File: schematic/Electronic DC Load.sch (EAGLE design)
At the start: 92 parts, among them J1 POWER_JACKPTH_LOCK, J2 AVR_SPI_PROG_3X22X3_LOCK, Q1 IRFP250NH, Q2 600mA/40V, U1 ATMEGA328P_TQFP, U2 PCF8574_DW_16, U3 REF5050_D_8, U4 INA210AIDCKRG4, U5 MP1584EN, U6 AD8629ARZ, U7 AD7190BRUZ, U8 AD5541ARZ, U9 LM35_LP_3, Y1 16MHz

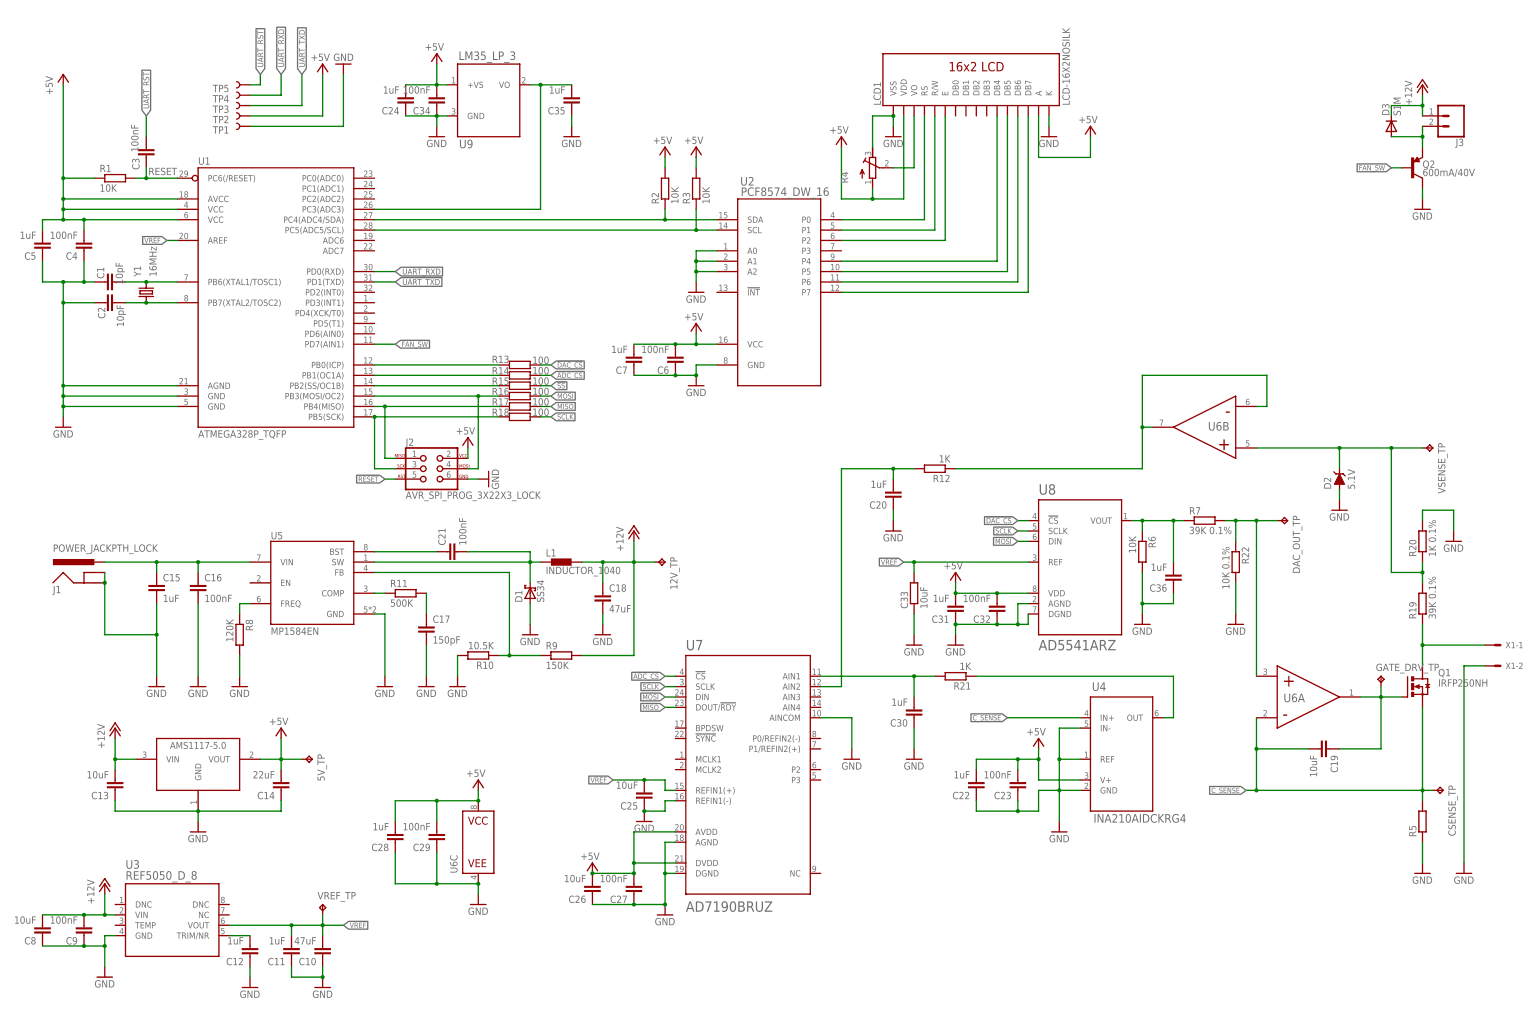
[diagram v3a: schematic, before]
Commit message: Add EC11 Rotary Encoder
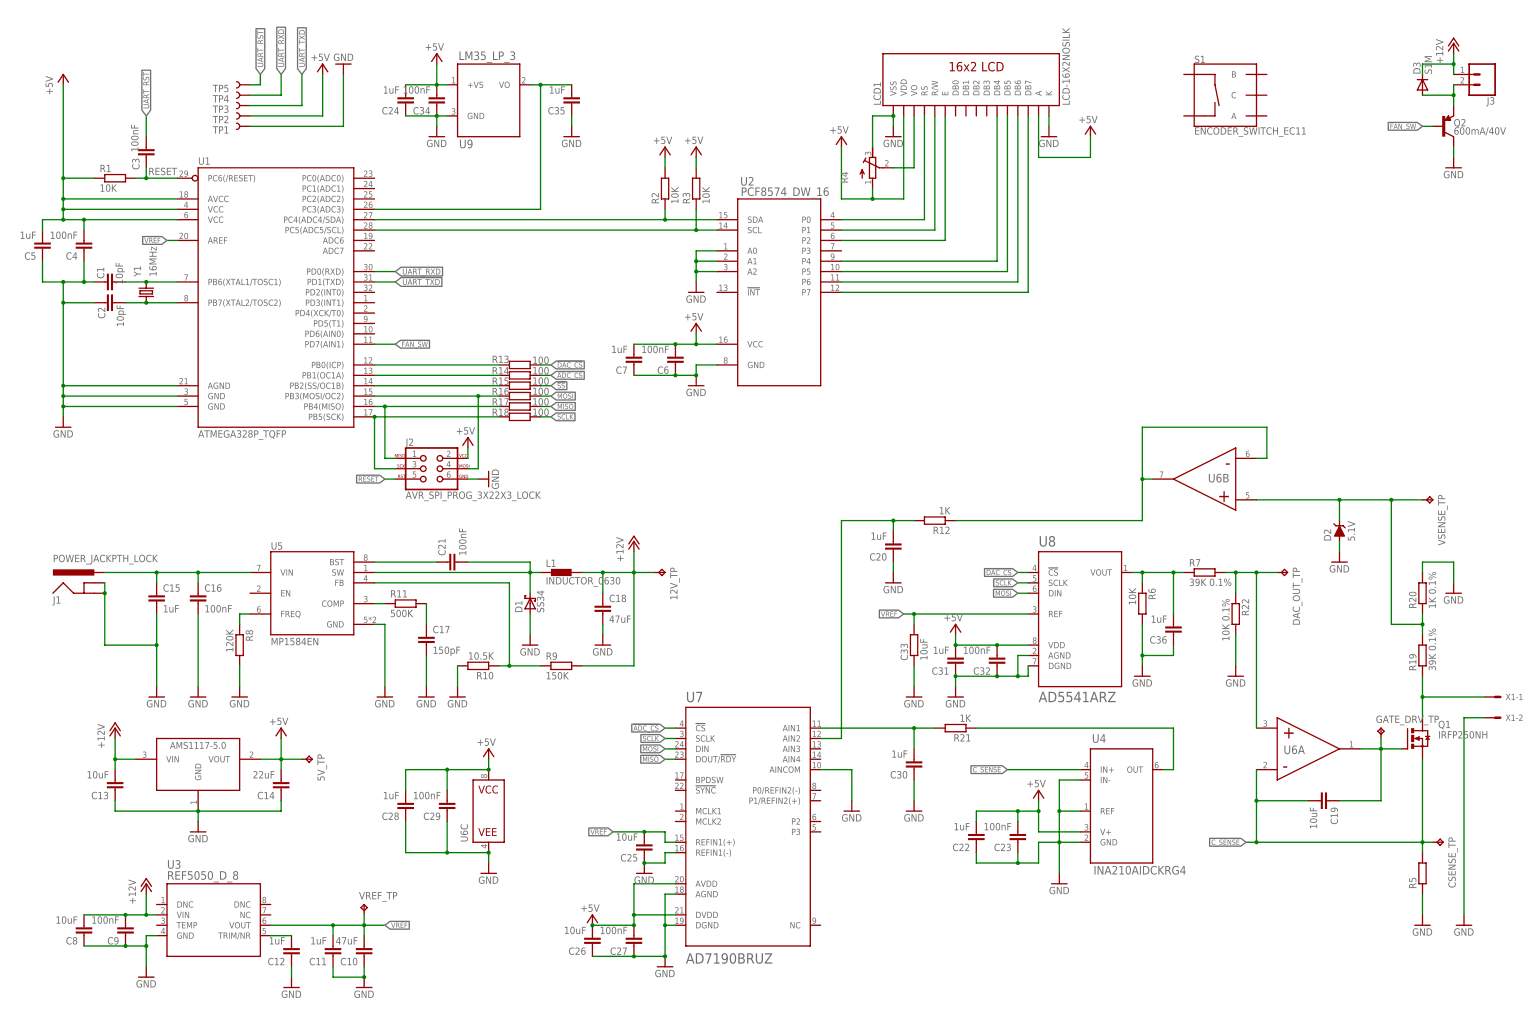
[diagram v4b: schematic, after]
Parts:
- added S1: ENCODER_SWITCH_EC11, 0_discrete:ENCODER_SWITCH_EC11
- L1: value INDUCTOR_1040 -> INDUCTOR_0630; device 0_discrete:INDUCTOR_1040 -> 0_discrete:INDUCTOR_0630
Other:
- moved on the sheet: 12V_TP, C10, C11, C12, C15, C16, C17, C18, C19, C20, C21, C22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

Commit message: First layouts
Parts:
- removed 5V_TP, CSENSE_TP, DAC_OUT_TP, GATE_DRV_TP, VREF_TP, VSENSE_TP: TPB2,54, testpad:TPB2,54
- removed TP1: TEST-POINT2, SparkFun-Connectors:TEST-POINT2
- removed TP2, TP3, TP4, TP5: TEST-POINT3, SparkFun-Connectors:TEST-POINT3
- removed U$1: AMS1117-5.0, AMS1117-5.0:AMS1117-5.0
- removed X1: (no value), con-molex:KK-156-2
- removed Y1: 16MHz, crystal-geyer_V1_0:KX-7
- added J4: KF762-2, 0_discrete:KF762-2
- added Q3: 600mA/40V, SparkFun-DiscreteSemi:TRANS_PNP-MMBT4403
- added R23, R24, R25, R26, R27, R28, R31, R32, R33: 10K, resistor:R-EU_R0603
- added R29, R30: 1K, resistor:R-EU_R0805
- added R34: 1uF, resistor:R-EU_R0805
- added R35: 39K 0.1%, resistor:R-EU_R0805
- added R36: 10K 0.1%, resistor:R-EU_R0805
- added R37: .005, 0_sup:MRE_R005_4W_2728_1%
- added R38: 39K 0.1%, resistor:R-EU_M0805
- added R39: 1K 0.1%, resistor:R-EU_M0805
- added S2, S3, S4, S5: SWITCH_6X6, 0_discrete:SWITCH_6X6
- added U10: AD8629ARZ, 0_analog-devices:AD8629ARZ
- added VR1: 10k, SparkFun-Resistors:TRIMPOT-SMD-3MM-OPEN-1/10W-25%
- C1: value 10pF -> 10uF; device resistor:C-EUC0603 -> resistor:C-EUC1206
- C10: device resistor:C-EUC0603 -> resistor:C-EUC1206
- C11, C34, C4, C5, C6: device resistor:C-EUC0603 -> resistor:C-EUC0805
- C12, C35: value 1uF -> 100nF; device resistor:C-EUC0603 -> resistor:C-EUC0805
- C13, C8: value 10uF -> 1uF; device resistor:C-EUC0603 -> resistor:C-EUC0805
- C14: value 22uF -> 150pF; device resistor:C-EUC0603 -> resistor:C-EUC0402
- C15, C24: value 1uF -> 100nF
- C17: value 150pF -> 1uF; device resistor:C-EUC1206 -> resistor:C-EUC0805
- C18: value 47uF -> 10uF
- C19: value 10uF -> 47uF; device resistor:C-EUC0603 -> resistor:C-EUC1206
- C2: value 10pF -> 100nF
- C20, C28: value 1uF -> 100nF; device resistor:C-EUC0805 -> resistor:C-EUC0603
- C21: device resistor:C-EUC1206 -> resistor:C-EUC0805
- C22: value 1uF -> 10uF; device resistor:C-EUC0805 -> resistor:C-EUC1206
- C23: device resistor:C-EUC0805 -> resistor:C-EUC0603
- C25, C26: value 10uF -> 100nF
- C29: value 100nF -> 1uF
- C3: value 100nF -> 10uF; device resistor:C-EUC0603 -> resistor:C-EUC1206
- C31, C36: value 1uF -> 10uF; device resistor:C-EUC0603 -> resistor:C-EUC1206
- C32, C9: value 100nF -> 1uF; device resistor:C-EUC0603 -> resistor:C-EUC0805
- C33: value 10uF -> 1uF; device resistor:R-EU_M1206 -> resistor:C-EUC0805
- C7: value 1uF -> 22uF; device resistor:C-EUC0603 -> resistor:C-EUC1206
- D1: value SS34 -> DIODE_SCHOTTKEYSS24; device diode:SCHOTTKY-DIODESMC -> 0_discrete:DIODE_SCHOTTKEYSS24
- J2: value AVR_SPI_PROG_3X22X3_LOCK -> AVR_SPI_PROG_3X2PTH; device SparkFun-Connectors:AVR_SPI_PROG_3X22X3_LOCK -> SparkFun-Connectors:AVR_SPI_PROG_3X2PTH
- J3: value (none) -> FAN
- Q1: value IRFP250NH -> 16MHz; device 0_discrete:IRFP250NH -> crystal-geyer_V1_0:KX-7
- Q2: value 600mA/40V -> IRFP250NV; device SparkFun-DiscreteSemi:TRANS_PNP-MMBT4403 -> 0_discrete:IRFP250NV
- R1, R2: value 10K -> 10pF; device resistor:R-EU_R0603 -> resistor:R-EU_R0805
- R10: value 10.5K -> 100; device resistor:R-EU_R0603 -> resistor:R-EU_M0805
- R11: value 500K -> 100; device resistor:R-EU_R0603 -> resistor:R-EU_M0805
- R12, R21: value 1K -> 10K; device resistor:R-EU_R0805 -> resistor:R-EU_R0603
- R13: value 100 -> 150K; device resistor:R-EU_M0805 -> resistor:R-EU_R0603
- R14, R15: value 100 -> 10K
- R16, R17, R18: value 100 -> 10K; device resistor:R-EU_M0805 -> resistor:R-EU_R0603
- R19: value 39K 0.1% -> 10K; device resistor:R-EU_M0805 -> resistor:R-EU_R0603
- R20: value 1K 0.1% -> 10K; device resistor:R-EU_M0805 -> resistor:R-EU_R0603
- R22: value 10K 0.1% -> 10K; device resistor:R-EU_R0805 -> resistor:R-EU_R0603
- R4: value (none) -> 120K; device resistor:R-TRIMM3296P -> resistor:R-EU_R0603
- R5: value (none) -> 500K; device 0_sup:MRE_R005_4W_2728_1% -> resistor:R-EU_R0603
- R6: value 10K -> 10.5K; device resistor:R-EU_R0805 -> resistor:R-EU_R0603
- R7: value 39K 0.1% -> 100; device resistor:R-EU_R0805 -> resistor:R-EU_M0805
- R8: value 120K -> 100; device resistor:R-EU_R0603 -> resistor:R-EU_M0805
- R9: value 150K -> 100; device resistor:R-EU_R0603 -> resistor:R-EU_M0805
- U1: value ATMEGA328P_TQFP -> AMS1117-5.0; device SparkFun-IC-Microcontroller:ATMEGA328P_TQFP -> AMS1117-5.0:AMS1117-5.0
- U2: value PCF8574_DW_16 -> REF5050_D_8; device 0_texas-instrument:PCF8574_DW_16 -> 0_texas-instrument:REF5050_D_8
- U3: value REF5050_D_8 -> ATMEGA328P_TQFP; device 0_texas-instrument:REF5050_D_8 -> SparkFun-IC-Microcontroller:ATMEGA328P_TQFP
- U4: value INA210AIDCKRG4 -> MP1584EN; device 0_texas-instrument:INA210AIDCKRG4 -> MP1584EN:MP1584EN
- U5: value MP1584EN -> LM35_LP_3; device MP1584EN:MP1584EN -> 0_texas-instrument:LM35_LP_3
- U6: value AD8629ARZ -> AD7190BRUZ; device 0_analog-devices:AD8629ARZ -> 0_analog-devices:AD7190BRUZ
- U7: value AD7190BRUZ -> AD5541ARZ; device 0_analog-devices:AD7190BRUZ -> 0_analog-devices:AD5541ARZ
- U8: value AD5541ARZ -> INA210AIDCKRG4; device 0_analog-devices:AD5541ARZ -> 0_texas-instrument:INA210AIDCKRG4
- U9: value LM35_LP_3 -> PCF8574_DW_16; device 0_texas-instrument:LM35_LP_3 -> 0_texas-instrument:PCF8574_DW_16
- renumbered 12V_TP to TP_12V
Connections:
- removed net !SS: R15.2
- removed net N$33: R15.1, U1.PB2(SS/OC1B)
- removed net UART_RST: C3.2, TP5.1
- removed net UART_RXD: TP4.1, U1.PD0(RXD)
- removed net UART_TXD: TP3.1, U1.PD1(TXD)
- removed net VCC: C4.2, C5.2, R1.1, TP2.1, U1.AVCC, U1.VCC@4, U1.VCC@6
- new net N$29: R21.1, R22.1, S1.B
- new net N$38: R23.1, R24.1, S1.A
- new net N$40: R17.2, R18.1, S2.1, S2.2
- new net N$41: R19.2, R20.1, S3.1, S3.2
- new net N$42: C20.2, R12.2, R16.1, S1.SW-
- new net N$43: C23.1, R17.1, U3.PD4(XCK/T0)
- new net N$44: R12.1, U3.PD2(INT0)
- new net N$46: C24.1, R19.1, U3.PD3(INT1)
- new net N$48: R27.2, R28.1, S5.1, S5.2
- new net N$51: R25.2, R26.1, S4.1, S4.2
- new net N$52: C26.1, R25.1, U3.PD5(T1)
- new net N$55: C27.1, R27.1, U3.PD6(AIN0)
- new net ROTARY_A: C28.1, R24.2, U3.PC0(ADC0)
- new net ROTARY_B: C25.1, R22.2, U3.PC1(ADC1)
- net !ADC_CS: now also R11.2, U6.!CS; no longer U7.!CS
- net !DAC_CS: now also R10.2, R15.2, U7.!CS; no longer R13.2, U8.!CS
- net +12V: now also C1.2, C19.1, C3.2, C4.2, R13.2, U1.VIN, U2.VIN; no longer C13.2, C18.1, C8.2, C9.2, R9.2, U$1.VIN, U3.VIN
- net +5V: now also C11.2, C12.2, C13.2, C15.2, C18.2, C2.2, C21.2, C33.2, C35.2, R14.1, R15.1, R16.2, R18.2, R20.2, R21.2, R23.2, R26.2, R28.2, R3.1, R31.2, R32.2, U1.VOUT, U10C.VCC, U3.AVCC, U3.VCC@4, U3.VCC@6, U5.+VS, U6.AVDD, U6.DVDD, U7.VDD, U8.V+, U9.VCC, VR1.CW; no longer 5V_TP.TP, C14.2, C22.2, C23.2, C24.2, C26.2, C27.2, C28.2, C29.2, C31.2, C6.2, R2.2, R3.2, R4.A, U$1.VOUT, U2.VCC, U4.V+, U6C.VCC, U7.AVDD, U7.DVDD, U8.VDD, U9.+VS
- net C_SENSE: now also C36.2, Q2.S, R37.2, U10A.IN-, U8.IN+; no longer C19.2, CSENSE_TP.TP, Q1.S, R5.2, U4.IN+, U6A.IN-
- net FAN_SW: now also Q3.B, U3.PD7(AIN1); no longer Q2.B, U1.PD7(AIN1)
- net GND: now also C14.2, C15.1, C17.1, C18.1, C19.2, C21.1, C23.2, C24.2, C25.2, C26.2, C27.2, C28.2, C3.1, C5.2, C6.2, J41.S, Q3.C, R1.1, R2.1, R33.2, R34.1, R36.2, R37.1, R39.2, R4.2, S1.C, S1.SW+, S2.3, S2.4, S3.3, S3.4, S4.3, S4.4, S5.3, S5.4, U1.GND, U10C.VEE, U3.AGND, U3.GND@3, U3.GND@5, U6.AGND, U6.AINCOM, U6.DGND, U6.REFIN1(-), U8.GND, U8.IN-, U8.REF, U9.A0, U9.A1, U9.A2, VR1.CCW; no longer C14.1, C15.2, C16.2, C17.2, C18.2, C23.1, C24.1, C25.1, C26.1, C27.1, C28.1, C36.1, C5.1, C6.1, Q2.C, R10.2, R20.2, R22.2, R4.E, R5.1, R8.2, TP1.1, U$1.GND, U1.AGND, U1.GND@3, U1.GND@5, U2.A0, U2.A1, U2.A2, U3.GND, U4.IN-, U4.REF, U6C.VEE, U7.AINCOM, U7.REFIN1(-), U8.AGND, U8.DGND, X1-2.S
- net MISO: now also R8.2, U6.DOUT/!RDY; no longer R17.2, U7.DOUT/!RDY
- net MOSI: now also R9.2, U6.DIN; no longer R16.2, U8.DIN
- net N$1: now also R31.1, U3.PC4(ADC4/SDA), U9.SDA; no longer R2.1, U1.PC4(ADC4/SDA), U2.SDA
- net N$10: now also C8.2, U2.TRIM/NR; no longer C12.2, U3.TRIM/NR
- net N$11: now also Q1.2, R2.2, U3.PB6(XTAL1/TOSC1); no longer C1.2, U1.PB6(XTAL1/TOSC1), Y1.2
- net N$12: now also Q1.1, R1.2, U3.PB7(XTAL2/TOSC2); no longer C2.2, U1.PB7(XTAL2/TOSC2), Y1.1
- net N$13: now also VR1.WIPER; no longer R4.S
- net N$14: now also J42.S, Q2.D, R38.1; no longer Q1.D, R19.1, X1-1.S
- net N$15: now also C17.2, U3.PC3(ADC3), U5.VO; no longer C35.2, U1.PC3(ADC3), U9.VO
- net N$16: now also C29.2, R29.2, U6.AIN1; no longer C20.2, R12.2, U7.AIN2
- net N$17: now also R4.1, U4.FREQ; no longer R8.1, U5.FREQ
- net N$18: now also R30.1, U8.OUT; no longer R21.1, U4.OUT
- net N$19: now also C16.1, U4.BST; no longer C21.1, U5.BST
- net N$2: now also R32.1, U3.PC5(ADC5/SCL), U9.SCL; no longer R3.1, U1.PC5(ADC5/SCL), U2.SCL
- net N$20: now also C5.1, C6.1, U4.VIN; no longer C15.1, C16.1, U5.VIN
- net N$21: now also C16.2, U4.SW; no longer C21.2, U5.SW
- net N$22: now also R13.1, R6.1, U4.FB; no longer R10.1, R9.1, U5.FB
- net N$23: now also R5.1, U4.COMP; no longer R11.1, U5.COMP
- net N$24: now also R30.2, U6.AIN2; no longer R21.2, U7.AIN1
- net N$25: now also C14.1, R5.2; no longer C17.1, R11.2
- net N$26: now also R33.1, R34.2, R35.1, U7.VOUT; no longer C36.2, R6.1, R7.1, U8.VOUT
- net N$27: now also R29.1, U10B.IN-, U10B.OUT; no longer R12.1, U6B.IN-, U6B.OUT
- net N$28: now also Q3.E; no longer Q2.E
- net N$3: now also U9.P4; no longer U2.P4
- net N$30: now also R7.1, U3.PB5(SCK); no longer R18.1, U1.PB5(SCK)
- net N$31: now also R8.1, U3.PB4(MISO); no longer R17.1, U1.PB4(MISO)
- net N$32: now also R9.1, U3.PB3(MOSI/OC2); no longer R16.1, U1.PB3(MOSI/OC2)
- net N$34: now also R10.1, U3.PB1(OC1A); no longer R14.1, U1.PB1(OC1A)
- net N$35: now also R11.1, U3.PB0(ICP); no longer R13.1, U1.PB0(ICP)
- net N$36: now also C36.1, Q2.G, U10A.OUT; no longer C19.1, GATE_DRV_TP.TP, Q1.G, U6A.OUT
- net N$37: now also R38.2, R39.1, U10B.IN+; no longer R19.2, R20.1, U6B.IN+, VSENSE_TP.TP
- net N$39: now also R35.2, R36.1, U10A.IN+; no longer DAC_OUT_TP.TP, R22.1, R7.2, U6A.IN+
- net N$4: now also U9.P5; no longer U2.P5
- net N$5: now also U9.P6; no longer U2.P6
- net N$6: now also U9.P7; no longer U2.P7
- net N$7: now also U9.P0; no longer U2.P0
- net N$8: now also U9.P1; no longer U2.P1
- net N$9: now also U9.P2; no longer U2.P2
- net RESET: now also R3.2, U3.PC6(/RESET); no longer C3.1, R1.2, U1.PC6(/RESET)
- net SCLK: now also R7.2, U6.SCLK; no longer R18.2, U8.SCLK
- net VREF: now also C22.2, C31.2, C9.2, U2.VOUT, U3.AREF, U6.REFIN1(+), U7.REF; no longer C11.2, C25.2, C33.2, U1.AREF, U3.VOUT, U7.REFIN1(+), U8.REF, VREF_TP.TP
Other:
- moved on the sheet: C1, C11, C12, C13, C14, C15, C16, C17, C18, C19, C2, C20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
